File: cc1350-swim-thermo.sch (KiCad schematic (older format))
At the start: 62 parts, among them P1 LMT_70_1, P2 LMT_70_2, P3 BNC, P4 USB_OTG, P5 CONN_02X05, Q1 2N7002, SW1 SW_Push, U1 2450BM14G0011T, U2 XMSSJE3G0PA-003, U3 CC1350F128RSM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

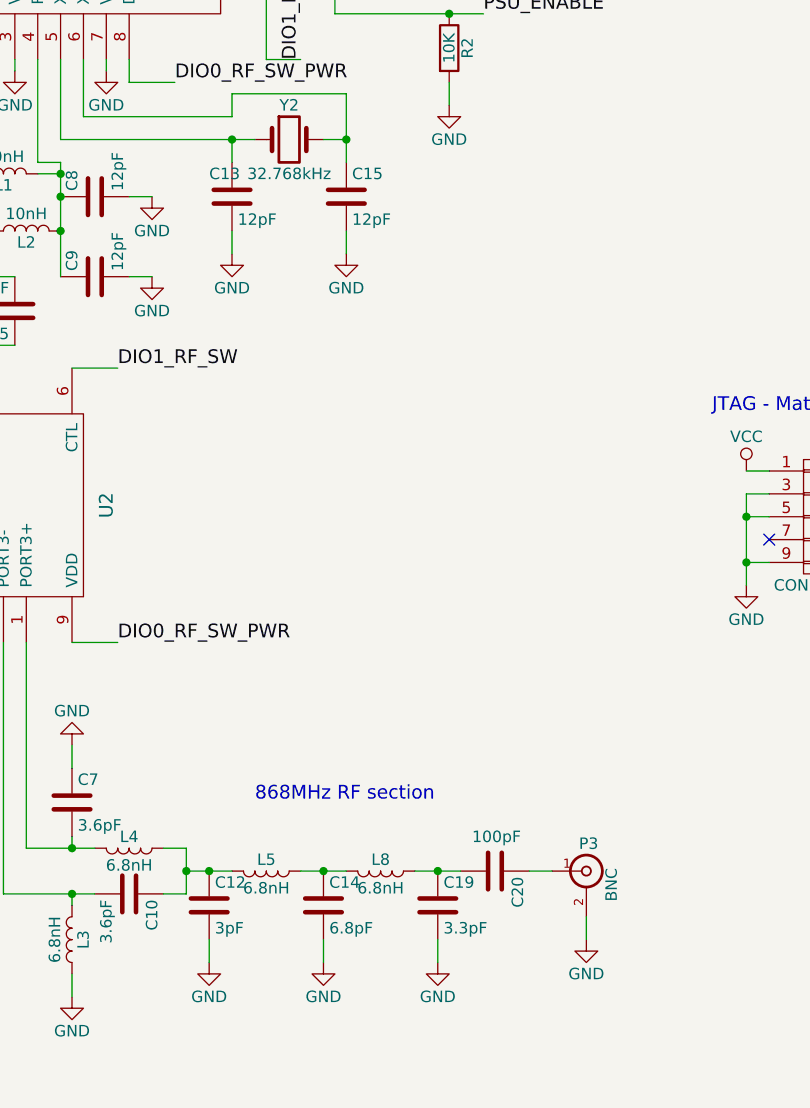
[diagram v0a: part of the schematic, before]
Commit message: started footprint association
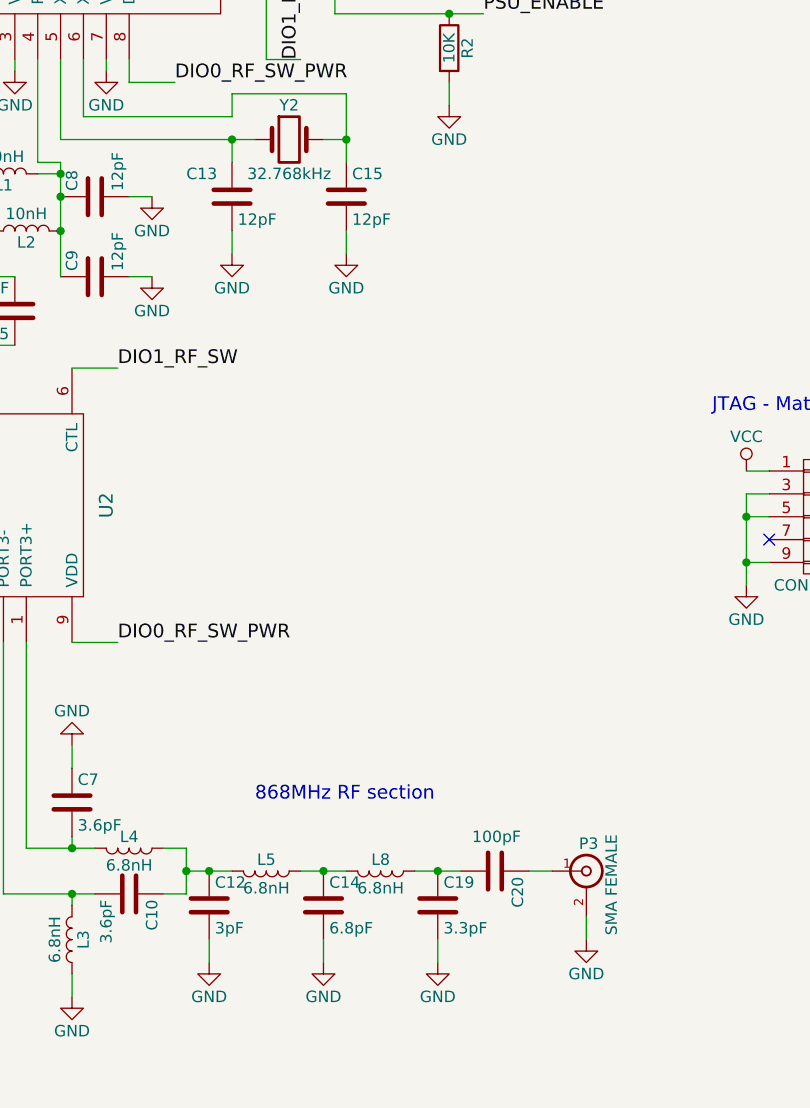
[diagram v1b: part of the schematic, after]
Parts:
- C1, C11, C13, C15, C16, C17, C18, C2, C21, C22, C23, C24, C25, C26, C3, C6: footprint (none) -> Capacitors_SMD:C_0603
- C10, C12, C14, C19, C20, C4, C5, C7, C8, C9: footprint (none) -> Capacitors_SMD:C_0402
- JP1: footprint (none) -> Pin_Headers:Pin_Header_Straight_1x02
- L6, L9, R1, R2, R3, R4, R5, R6, R7: footprint (none) -> Resistors_SMD:R_0603
- L7: footprint (none) -> Resistors_SMD:R_0805
- P1, P2: footprint (none) -> Connectors_Molex:Molex_KK-6410-04_04x2.54mm_Straight
- P3: value BNC -> SMA FEMALE
- Q1: footprint (none) -> TO_SOT_Packages_SMD:SOT-23

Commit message: associated standard components
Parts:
- D1: footprint (none) -> LEDs:LED_WS2812B-PLCC4
- L1, L2, L3, L4, L5, L8: footprint (none) -> Resistors_SMD:R_0402
- P4: footprint (none) -> Connectors:USB_Mini-B
- U4: footprint (none) -> TO_SOT_Packages_SMD:SOT-23-5
- U5: footprint (none) -> Housings_SOIC:SOIC-8_3.9x4.9mm_Pitch1.27mm
- U6: footprint (none) -> TO_SOT_Packages_SMD:SOT-23-6
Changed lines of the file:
@@
 F 0 "U5" H 9400 3600 60  0000 C CNN
 F 1 "TLC5973" H 9400 3000 60  0000 C CNN
-F 2 "" H 9400 3300 60  0001 C CNN
+F 2 "Housings_SOIC:SOIC-8_3.9x4.9mm_Pitch1.27mm" H 9400 3300 60  0001 C CNN
 F 3 "" H 9400 3300 60  0001 C CNN
 	1    9400 3300
@@
 F 0 "U6" H 9650 5700 60  0000 C CNN
 F 1 "MCP16251" H 9650 5200 60  0000 C CNN
-F 2 "" H 9650 5450 60  0001 C CNN
+F 2 "TO_SOT_Packages_SMD:SOT-23-6" H 9650 5450 60  0001 C CNN
 F 3 "" H 9650 5450 60  0001 C CNN
 	1    9650 5450
@@
 F 0 "U4" H 8750 2150 60  0000 C CNN
 F 1 "TLV713" H 8750 1650 60  0000 C CNN
-F 2 "" H 8750 1700 60  0001 C CNN
+F 2 "TO_SOT_Packages_SMD:SOT-23-5" H 8750 1700 60  0001 C CNN
 F 3 "" H 8750 1700 60  0001 C CNN
 	1    8750 1900
@@
 F 0 "L2" V 4050 3900 50  0000 C CNN
 F 1 "10nH" V 4175 3900 50  0000 C CNN
-F 2 "" H 4100 3900 50  0001 C CNN
+F 2 "Resistors_SMD:R_0402" H 4100 3900 50  0001 C CNN
 F 3 "" H 4100 3900 50  0000 C CNN
 	1    4100 3900
@@
 F 0 "L1" V 3950 3650 50  0000 C CNN
 F 1 "10nH" V 4075 3650 50  0000 C CNN
-F 2 "" H 4000 3650 50  0001 C CNN
+F 2 "Resistors_SMD:R_0402" H 4000 3650 50  0001 C CNN
 F 3 "" H 4000 3650 50  0000 C CNN
 	1    4000 3650
@@
 F 0 "L8" V 5600 6700 50  0000 C CNN
 F 1 "6.8nH" V 5725 6700 50  0000 C CNN
-F 2 "" H 5650 6700 50  0001 C CNN
+F 2 "Resistors_SMD:R_0402" H 5650 6700 50  0001 C CNN
 F 3 "" H 5650 6700 50  0000 C CNN
 	1    5650 6700
@@
 F 0 "L5" V 5100 6700 50  0000 C CNN
 F 1 "6.8nH" V 5225 6700 50  0000 C CNN
-F 2 "" H 5150 6700 50  0001 C CNN
+F 2 "Resistors_SMD:R_0402" H 5150 6700 50  0001 C CNN
 F 3 "" H 5150 6700 50  0000 C CNN
 	1    5150 6700
@@
 F 0 "L3" V 4250 7000 50  0000 C CNN
 F 1 "6.8nH" V 4375 7000 50  0000 C CNN
-F 2 "" H 4300 7000 50  0001 C CNN
+F 2 "Resistors_SMD:R_0402" H 4300 7000 50  0001 C CNN
 F 3 "" H 4300 7000 50  0000 C CNN
 	1    4300 7000
@@
 F 0 "L4" V 4500 6600 50  0000 C CNN
 F 1 "6.8nH" V 4625 6600 50  0000 C CNN
-F 2 "" H 4550 6600 50  0001 C CNN
+F 2 "Resistors_SMD:R_0402" H 4550 6600 50  0001 C CNN
 F 3 "" H 4550 6600 50  0000 C CNN
 	1    4550 6600
@@
 F 0 "D1" H 8500 3620 50  0000 C CNN
 F 1 "CLV1A-FKB" H 8500 2900 50  0000 C CNN
-F 2 "" H 8500 3200 50  0001 C CNN
+F 2 "LEDs:LED_WS2812B-PLCC4" H 8500 3200 50  0001 C CNN
 F 3 "" H 8500 3200 50  0000 C CNN
 	1    8500 3250
@@
 F 0 "P4" H 7025 1475 50  0000 C CNN
 F 1 "USB_OTG" H 6700 1800 50  0000 C CNN
-F 2 "" V 6650 1500 50  0001 C CNN
+F 2 "Connectors:USB_Mini-B" V 6650 1500 50  0001 C CNN
 F 3 "" V 6650 1500 50  0000 C CNN
 	1    6700 1600

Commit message: made some footprints
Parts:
- removed AE1: Antenna_Shield, symbol Antenna_Shield
- added AE1: Antenna, cc1350:2450AT42A100, symbol Antenna
- BT1: footprint (none) -> cc1350:2_AAA_batteryholder_keystone
- L10: footprint (none) -> cc1350:VLS3015E
- P3: footprint (none) -> cc1350:sma_female_top
- P5: footprint (none) -> cc1350:Pin_Header_Straight_SMT_02x05_1_27mm
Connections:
- wire segments 197 -> 196

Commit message: made all footprints
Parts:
- SW1: footprint (none) -> cc1350:SKSLLAE010
- U1: footprint (none) -> cc1350:2450BM14G011T
- U2: footprint (none) -> cc1350:XMSSJE3G0PA-003
- U3: footprint (none) -> cc1350:CC1350F128RSM
- Y1: footprint (none) -> cc1350:TSX-3225
- Y2: footprint (none) -> cc1350:FC-135
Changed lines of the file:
@@
 F 0 "U3" H 4150 2450 60  0000 C CNN
 F 1 "CC1350F128RSM" H 4200 2300 60  0000 C CNN
-F 2 "" H 4400 2050 60  0001 C CNN
+F 2 "cc1350:CC1350F128RSM" H 4400 2050 60  0001 C CNN
 F 3 "" H 4400 2050 60  0001 C CNN
 	1    4150 2350
@@
 F 0 "U2" H 3900 5650 60  0000 C CNN
 F 1 "XMSSJE3G0PA-003" H 3900 4500 60  0000 C CNN
-F 2 "" H 3750 4700 60  0001 C CNN
+F 2 "cc1350:XMSSJE3G0PA-003" H 3750 4700 60  0001 C CNN
 F 3 "" H 3750 4700 60  0001 C CNN
 	1    3900 5100
@@
 F 0 "Y2" H 5250 3650 50  0000 C CNN
 F 1 "32.768kHz" H 5250 3350 50  0000 C CNN
-F 2 "" H 5250 3500 50  0001 C CNN
+F 2 "cc1350:FC-135" H 5250 3500 50  0001 C CNN
 F 3 "" H 5250 3500 50  0000 C CNN
 	1    5250 3500
@@
 F 0 "U1" H 3350 7500 60  0000 C CNN
 F 1 "2450BM14G0011T" H 3350 5800 60  0000 C CNN
-F 2 "" H 3150 6650 60  0001 C CNN
+F 2 "cc1350:2450BM14G011T" H 3150 6650 60  0001 C CNN
 F 3 "" H 3150 6650 60  0001 C CNN
 	1    3350 6650
@@
 F 0 "Y1" H 2300 3350 50  0000 L CNN
 F 1 "24MHz" H 2150 3250 50  0000 L CNN
-F 2 "" H 2550 3450 50  0001 C CNN
+F 2 "cc1350:TSX-3225" H 2550 3450 50  0001 C CNN
 F 3 "" H 2550 3450 50  0000 C CNN
 	1    2550 3450
@@
 F 0 "SW1" H 1300 1850 50  0000 L CNN
 F 1 "SW_Push" H 1250 1690 50  0000 C CNN
-F 2 "" H 1250 1950 50  0001 C CNN
+F 2 "cc1350:SKSLLAE010" H 1250 1950 50  0001 C CNN
 F 3 "" H 1250 1950 50  0000 C CNN
 	1    1250 1750

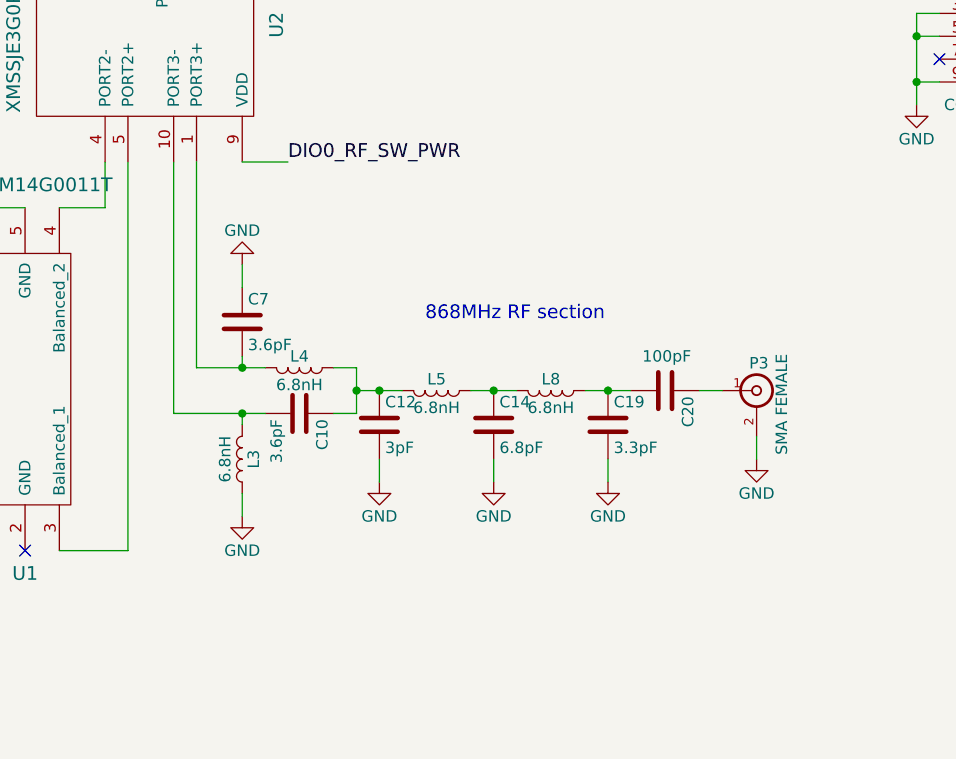
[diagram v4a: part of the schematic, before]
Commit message: changed balun to LFB18868MBG9E212
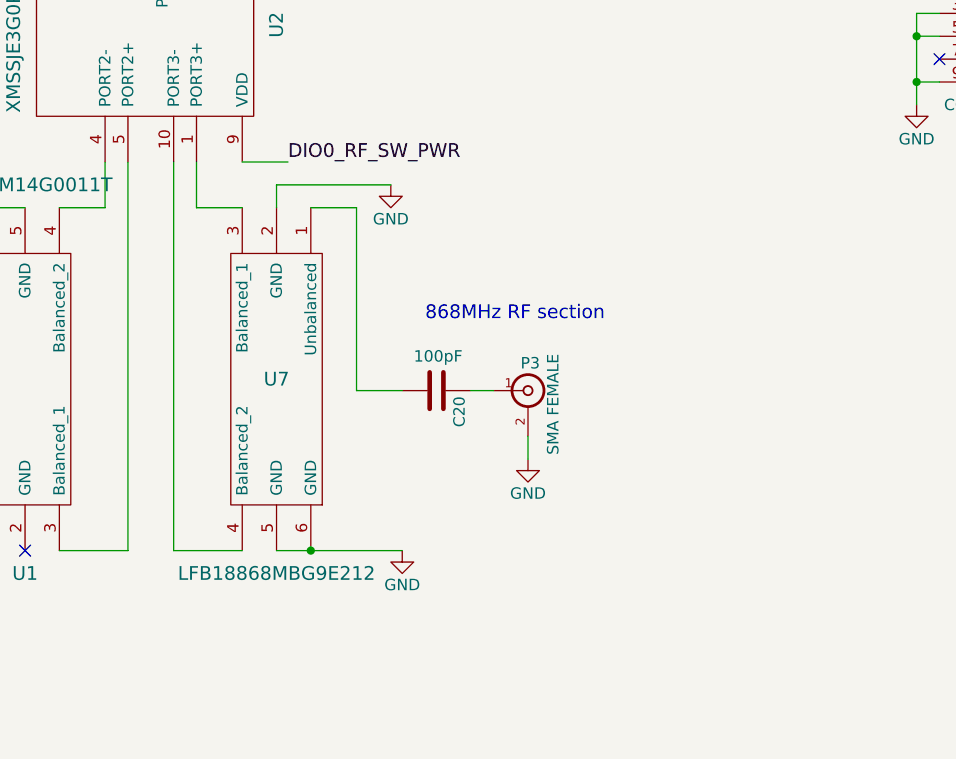
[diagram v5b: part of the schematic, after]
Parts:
- removed C10, C7: 3.6pF, Capacitors_SMD:C_0402, symbol C
- removed C12: 3pF, Capacitors_SMD:C_0402, symbol C
- removed C14: 6.8pF, Capacitors_SMD:C_0402, symbol C
- removed C19: 3.3pF, Capacitors_SMD:C_0402, symbol C
- removed L3, L4, L5, L8: 6.8nH, Resistors_SMD:R_0402, symbol L
- added U7: LFB18868MBG9E212, cc1350:LFB18868MBG9E212, symbol LFB18868MBG9E212
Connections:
- net GND: now also U7.2 (GND), U7.5 (GND), U7.6 (GND)
- net at U2.1 (PORT3+): now also U7.3 (Balanced_1)
- net at U2.10 (PORT3-): now also U7.4 (Balanced_2)
- net at C20.2: now also U7.1 (Unbalanced)
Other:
- moved on the sheet: C20, P3

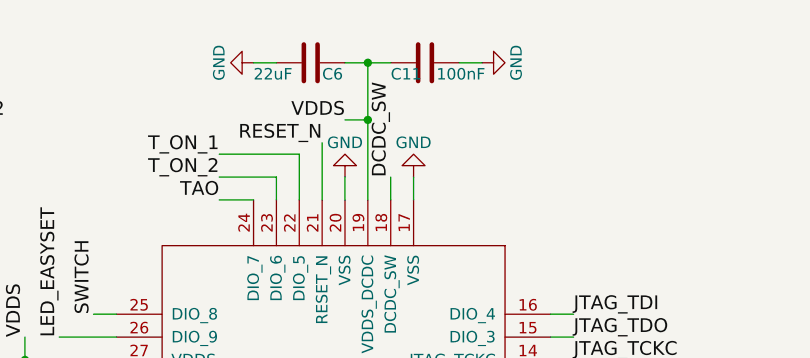
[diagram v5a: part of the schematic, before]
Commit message: placed all footprints and new board edge
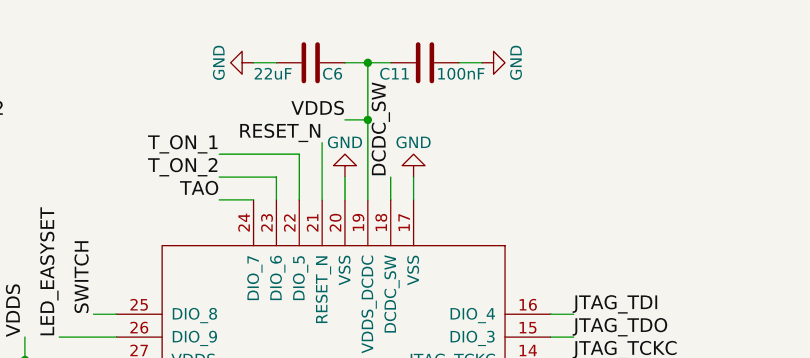
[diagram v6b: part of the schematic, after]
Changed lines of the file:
@@
 U 1 1 58C5C292
 P 4600 850
-F 0 "C11" V 4650 700 50  0000 L CNN
+F 0 "C11" V 4650 650 50  0000 L CNN
 F 1 "100nF" V 4650 900 50  0000 L CNN
 F 2 "Capacitors_SMD:C_0603" H 4638 700 50  0001 C CNN

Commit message: started wiring
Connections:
- net GND: now also U1.2 (GND)
- no-connect marks 8 -> 7
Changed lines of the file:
@@
 U 1 1 58C40E34
 P 3350 6650
-F 0 "U1" H 3350 7500 60  0000 C CNN
+F 0 "U1" H 3350 6650 60  0000 C CNN
 F 1 "2450BM14G0011T" H 3350 5800 60  0000 C CNN
 F 2 "cc1350:2450BM14G011T" H 3150 6650 60  0001 C CNN
@@
 	1    0    0    -1
 $EndComp
-NoConn ~ 3350 7400
 NoConn ~ 5300 12700
 $Comp
@@
 Wire Wire Line
 	4800 6700 5000 6700
+$Comp
+L GND #PWR?
+U 1 1 58D96477
+P 3350 7550
+F 0 "#PWR?" H 3350 7300 50  0001 C CNN
+F 1 "GND" H 3350 7400 50  0000 C CNN
+F 2 "" H 3350 7550 50  0000 C CNN
+F 3 "" H 3350 7550 50  0000 C CNN
+	1    3350 7550
+	1    0    0    -1
+$EndComp
+Wire Wire Line
+	3350 7400 3350 7550
 $EndSCHEMATC
